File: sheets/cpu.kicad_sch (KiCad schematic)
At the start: 6 parts, among them J1 BEER, U1 uPD43256AGU-12L, U2 uPD43256AGU-12L, U3 HD68HC000P, U4 NEO-C1

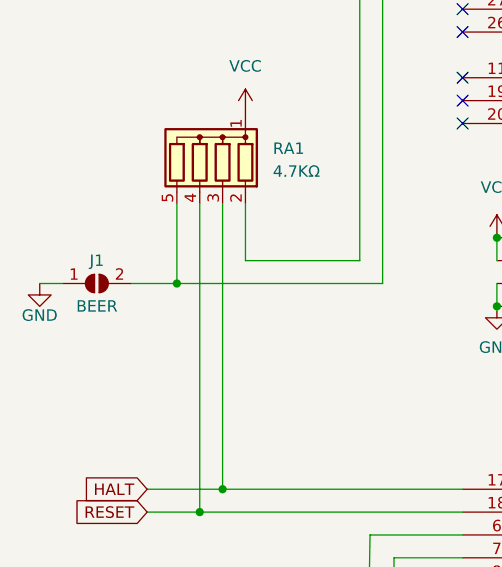
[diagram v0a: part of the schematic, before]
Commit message: Upgrade Schematics to Kicad 7.0
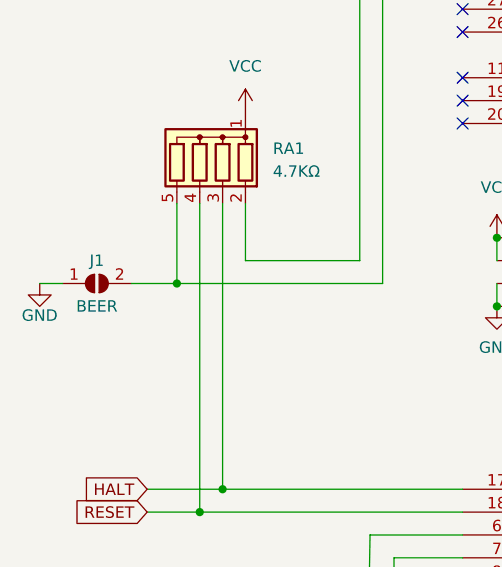
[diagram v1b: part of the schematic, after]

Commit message: Schematics Footprint updates
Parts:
- RA1: footprint Resistor_THT:R_Array_SIP5 -> 1_NeoGeoLibrary:R_Array_SIP5
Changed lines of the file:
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@@
       (effects (font (size 1.27 1.27)) (justify right))
     )
-    (property "Footprint" "Resistor_THT:R_Array_SIP5" (at 53.467 140.208 90)
+    (property "Footprint" "1_NeoGeoLibrary:R_Array_SIP5" (at 53.467 140.208 90)
       (effects (font (size 1.27 1.27)) hide)
     )

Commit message: Final update to Schematics Footprints Silkscreens
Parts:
- RA1: value 4.7KΩ -> 4.7ΩX4
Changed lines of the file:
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@@
   (symbol (lib_id "Device:R_Network04") (at 60.452 140.208 0) (mirror y) (unit 1)
     (in_bom yes) (on_board yes) (dnp no) (fields_autoplaced)
-    (property "Reference" "RA1" (at 68.58 139.1919 0)
+    (property "Reference" "RA1" (at 68.58 139.827 0)
       (effects (font (size 1.27 1.27)) (justify right))
     )
-    (property "Value" "4.7KΩ" (at 68.58 141.7319 0)
+    (property "Value" "4.7ΩX4" (at 68.58 142.367 0)
       (effects (font (size 1.27 1.27)) (justify right))
     )

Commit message: Some tweaks
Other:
- company: (none) -> SNK
- title: (none) -> NeoGeo AES
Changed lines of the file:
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@@
 (kicad_sch (version 20230121) (generator eeschema)
   (paper "A3")
+  (title_block
+    (title "NeoGeo AES")
+    (date "2023-08-19")
+    (rev "3.5")
+    (company "SNK")
+    (comment 3 "https://github.com/Board-Folk")
+    (comment 4 "Recreated By The Board Folk Team")
+  )
   (junction (at 174.498 45.593) (diameter 0) (color 0 0 0 0)
   )

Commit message: Updates to PCB Move P2 Joystick Port Move Memory Card Move Holes at top right Silkscreen added Update Titles
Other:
- title: NeoGeo AES -> NeoGeo AES 3-5
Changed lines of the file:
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@@
   (paper "A3")
   (title_block
-    (title "NeoGeo AES")
-    (date "2023-08-19")
-    (rev "3.5")
+    (title "NeoGeo AES 3-5")
+    (date "2023-08-27")
+    (rev "BF1.1")
     (company "SNK")
     (comment 3 "https://github.com/Board-Folk")

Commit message: More silkscreen tidy up, adding mouser components to BOM
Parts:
- RA1: value 4.7ΩX4 -> 4.7Kx4
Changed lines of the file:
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@@
   (symbol (lib_id "Device:R_Network04") (at 60.452 140.208 0) (mirror y) (unit 1)
     (in_bom yes) (on_board yes) (dnp no) (fields_autoplaced)
-    (property "Reference" "RA1" (at 68.58 139.827 0)
+    (property "Reference" "RA1" (at 68.58 139.192 0)
       (effects (font (size 1.27 1.27)) (justify right))
     )
-    (property "Value" "4.7ΩX4" (at 68.58 142.367 0)
+    (property "Value" "4.7Kx4" (at 68.58 141.732 0)
       (effects (font (size 1.27 1.27)) (justify right))
     )

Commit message: Little tweaks to silkscreen Updated BOM with mouser parts
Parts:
- J1: now left out of the parts list
- RA1: Mouser (none) -> 652-4605X-1LF-47K
- U1, U2, U3, U4: Comment (none) -> Use Original
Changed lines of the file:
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@@
     (title "NeoGeo AES 3-5")
     (date "2023-08-27")
-    (rev "BF1.1")
+    (rev "BF1.2")
     (company "SNK")
     (comment 3 "https://github.com/Board-Folk")
@@
       (effects (font (size 1.27 1.27)) hide)
     )
-    (property "Mouser" "" (at 60.452 140.208 0)
+    (property "Mouser" "652-4605X-1LF-47K" (at 60.452 140.208 0)
+      (effects (font (size 1.27 1.27)) hide)
+    )
+    (property "Alternative" "" (at 60.452 140.208 0)
       (effects (font (size 1.27 1.27)) hide)
     )
@@
   )
   (symbol (lib_id "Jumper:SolderJumper_2_Open") (at 49.022 154.178 0) (unit 1)
-    (in_bom yes) (on_board yes) (dnp no)
+    (in_bom no) (on_board yes) (dnp no)
     (property "Reference" "J1" (at 49.022 151.638 0)
       (effects (font (size 1.27 1.27)))
@@
     )
     (property "Mouser" "" (at 49.022 154.178 0)
+      (effects (font (size 1.27 1.27)) hide)
+    )
+    (property "Alternative" "" (at 49.022 154.178 0)
       (effects (font (size 1.27 1.27)) hide)
     )
@@
     )
     (property "Mouser" "" (at 304.038 114.3 0)
+      (effects (font (size 1.27 1.27)) hide)
+    )
+    (property "Comment" "Use Original" (at 304.038 114.3 0)
+      (effects (font (size 1.27 1.27)) hide)
+    )
+    (property "Alternative" "" (at 304.038 114.3 0)
       (effects (font (size 1.27 1.27)) hide)
     )
@@
       (effects (font (size 1.27 1.27)) hide)
     )
+    (property "Alternative" "" (at 197.612 118.618 0)
+      (effects (font (size 1.27 1.27)) hide)
+    )
+    (property "Comment" "Use Original" (at 197.612 118.618 0)
+      (effects (font (size 1.27 1.27)) hide)
+    )
     (pin "1")
     (pin "10")
@@
       (effects (font (size 1.27 1.27)) hide)
     )
+    (property "Alternative" "" (at 197.612 169.672 0)
+      (effects (font (size 1.27 1.27)) hide)
+    )
+    (property "Comment" "Use Original" (at 197.612 169.672 0)
+      (effects (font (size 1.27 1.27)) hide)
+    )
     (pin "1")
     (pin "10")
@@
       (effects (font (size 1.27 1.27)) hide)
     )
+    (property "Comment" "Use Original" (at 115.062 146.558 0)
+      (effects (font (size 1.27 1.27)) hide)
+    )
+    (property "Alternative" "" (at 115.062 146.558 0)
+      (effects (font (size 1.27 1.27)) hide)
+    )
